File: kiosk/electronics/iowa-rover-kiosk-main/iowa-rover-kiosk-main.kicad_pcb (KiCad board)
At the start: 2 copper layers, 76.8 x 79.9 mm, 17 parts, among them J2 Barrel_Jack, J3 Conn_02x06_Odd_Even, J4 Conn_01x04, J5 Conn_02x08_Top_Bottom, J6 Conn_01x08, J7 Conn_01x03, U1 Adafruit_RFM69HCW_Breakout, U2 I50115, U3 ATtiny84-20P

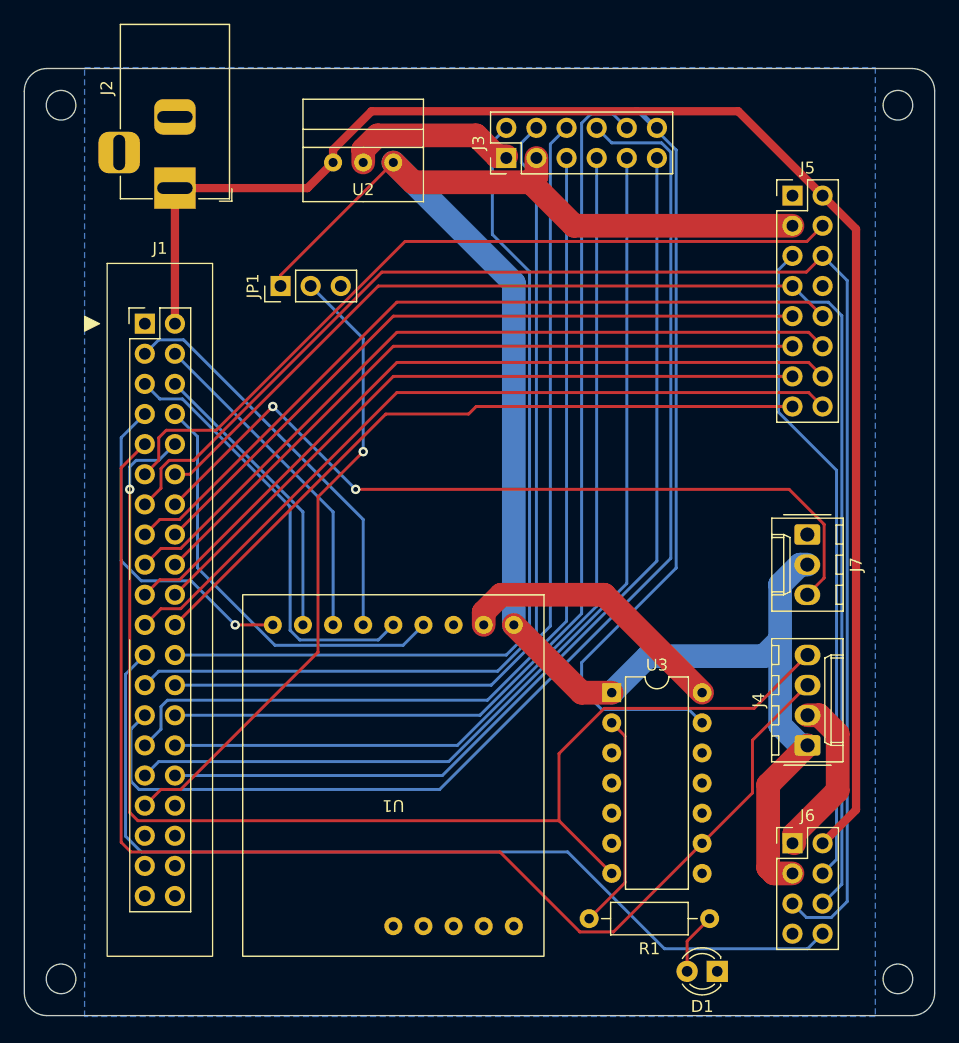
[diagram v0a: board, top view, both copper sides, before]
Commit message: initial pass at board drawings
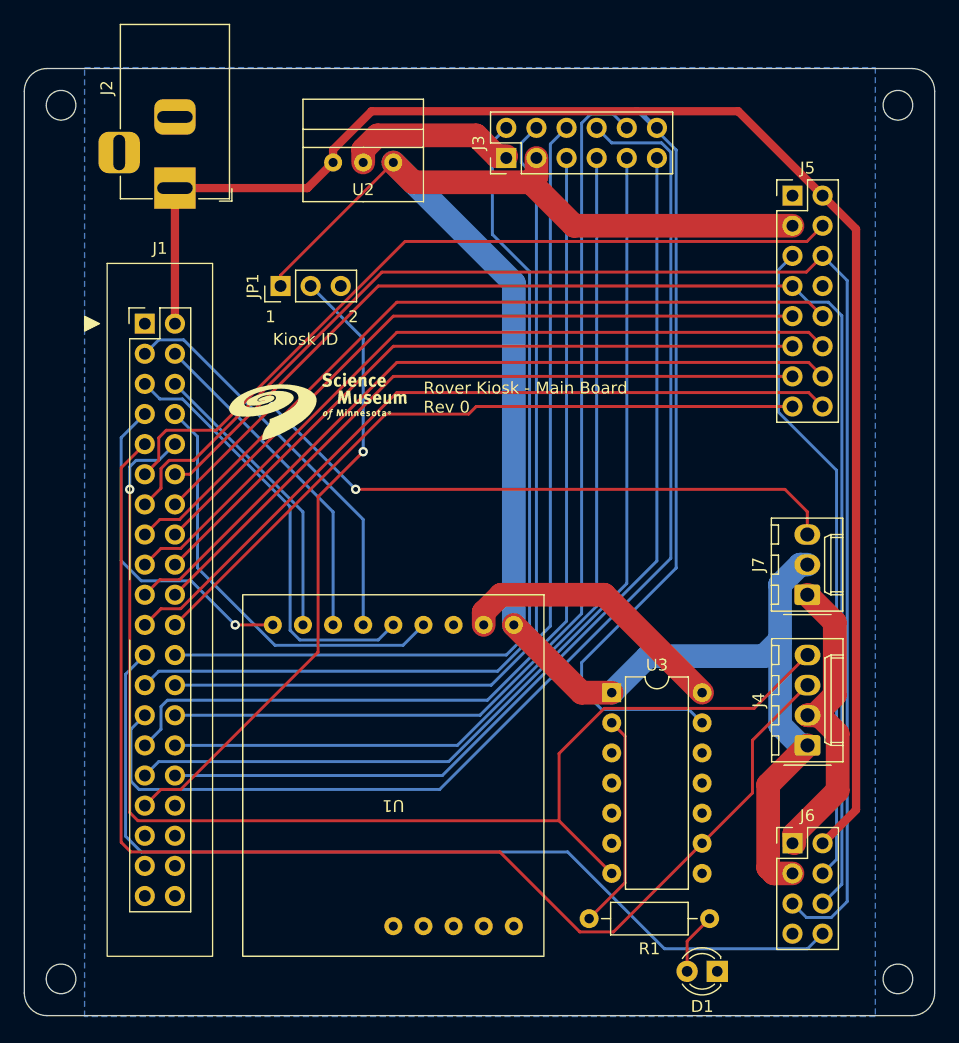
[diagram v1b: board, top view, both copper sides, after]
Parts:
- added G***: LOGO, SMM:smm-logo-15mm, F.Cu at (62.2, 75.6)
- moved J7 5.08 mm to (103.5, 91.4), turned to 90 degrees
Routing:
- net GND: track 51.8 -> 64.3 mm
- net Net-(J1-D6_NEO): track 68.8 -> 62.3 mm
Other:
- board text added: "1"
- board text added: "2"
- board text added: "Kiosk ID"
- board text added: "Rover Kiosk - Main Board Rev 0"

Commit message: update
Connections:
- U3 pad 7: /SCL -> /SDA
- U3 pad 9: /SDA -> /SCL
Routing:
- net /SDA: track 106.6 -> 74.2 mm
- net /SCL: track 106.6 -> 91.0 mm
- net +5V: track 154.1 -> 154.8 mm
- net Net-(J1-D45_RST): track 28.1 -> 28.7 mm
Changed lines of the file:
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@@
       (net 57 "unconnected-(U3-PA7-Pad6)") (pinfunction "PA7") (pintype "bidirectional+no_connect"))
     (pad "7" thru_hole oval (at 0 15.24) (size 1.6 1.6) (drill 0.8) (layers "*.Cu" "*.Mask")
-      (net 11 "/SCL") (pinfunction "PA6") (pintype "bidirectional"))
+      (net 10 "/SDA") (pinfunction "PA6") (pintype "bidirectional"))
     (pad "8" thru_hole oval (at 7.62 15.24) (size 1.6 1.6) (drill 0.8) (layers "*.Cu" "*.Mask")
       (net 58 "unconnected-(U3-PA5-Pad8)") (pinfunction "PA5") (pintype "bidirectional+no_connect"))
     (pad "9" thru_hole oval (at 7.62 12.7) (size 1.6 1.6) (drill 0.8) (layers "*.Cu" "*.Mask")
-      (net 10 "/SDA") (pinfunction "PA4") (pintype "bidirectional"))
+      (net 11 "/SCL") (pinfunction "PA4") (pintype "bidirectional"))
     (pad "10" thru_hole oval (at 7.62 10.16) (size 1.6 1.6) (drill 0.8) (layers "*.Cu" "*.Mask")
       (net 59 "unconnected-(U3-PA3-Pad10)") (pinfunction "PA3") (pintype "bidirectional+no_connect"))
@@
   (segment (start 58.42 93.98) (end 55.335 93.98) (width 0.25) (layer "F.Cu") (net 8))
   (via (at 55.245 93.98) (size 0.8) (drill 0.4) (layers "F.Cu" "B.Cu") (net 8))
-  (segment (start 55.245 93.98) (end 51.53 90.265) (width 0.25) (layer "B.Cu") (net 8))
-  (segment (start 47.328299 90.265) (end 45.63 88.566701) (width 0.25) (layer "B.Cu") (net 8))
-  (segment (start 45.63 78.195) (end 47.625 76.2) (width 0.25) (layer "B.Cu") (net 8))
-  (segment (start 45.63 88.566701) (end 45.63 78.195) (width 0.25) (layer "B.Cu") (net 8))
-  (segment (start 51.53 90.265) (end 47.328299 90.265) (width 0.25) (layer "B.Cu") (net 8))
+  (segment (start 47.233299 90.17) (end 51.435 90.17) (width 0.25) (layer "B.Cu") (net 8))
+  (segment (start 51.435 90.17) (end 55.245 93.98) (width 0.25) (layer "B.Cu") (net 8))
+  (segment (start 47.625 76.2) (end 44.995 78.83) (width 0.25) (layer "B.Cu") (net 8))
+  (segment (start 44.995 78.83) (end 44.995 87.931701) (width 0.25) (layer "B.Cu") (net 8))
+  (segment (start 44.995 87.931701) (end 47.233299 90.17) (width 0.25) (layer "B.Cu") (net 8))
   (segment (start 69.4 95.7) (end 58.602749 95.7) (width 0.25) (layer "B.Cu") (net 9))
   (segment (start 71.12 93.98) (end 69.4 95.7) (width 0.25) (layer "B.Cu") (net 9))
@@
   (segment (start 58.602749 95.7) (end 52.069302 89.166553) (width 0.25) (layer "B.Cu") (net 9))
   (segment (start 52.069302 89.166553) (end 52.069302 78.104302) (width 0.25) (layer "B.Cu") (net 9))
-  (segment (start 45.63 112.305) (end 46.45 113.125) (width 0.25) (layer "F.Cu") (net 10))
-  (segment (start 98.86 108.15) (end 98.86 103.705) (width 0.25) (layer "F.Cu") (net 10))
-  (segment (start 84.31 119.87) (end 87.14 119.87) (width 0.25) (layer "F.Cu") (net 10))
-  (segment (start 47.625 78.74) (end 45.63 80.735) (width 0.25) (layer "F.Cu") (net 10))
-  (segment (start 98.86 103.705) (end 103.505 99.06) (width 0.25) (layer "F.Cu") (net 10))
-  (segment (start 45.63 80.735) (end 45.63 112.305) (width 0.25) (layer "F.Cu") (net 10))
-  (segment (start 46.45 113.125) (end 77.565 113.125) (width 0.25) (layer "F.Cu") (net 10))
-  (segment (start 94.615 112.395) (end 98.86 108.15) (width 0.25) (layer "F.Cu") (net 10))
-  (segment (start 77.565 113.125) (end 84.31 119.87) (width 0.25) (layer "F.Cu") (net 10))
-  (segment (start 87.14 119.87) (end 94.615 112.395) (width 0.25) (layer "F.Cu") (net 10))
-  (segment (start 82.55 110.49) (end 86.995 114.935) (width 0.25) (layer "F.Cu") (net 11))
-  (segment (start 86.36 101.02) (end 99.005 101.02) (width 0.25) (layer "F.Cu") (net 11))
-  (segment (start 82.55 110.49) (end 82.55 104.83) (width 0.25) (layer "F.Cu") (net 11))
-  (segment (start 46.355 82.55) (end 46.355 109.801701) (width 0.25) (layer "F.Cu") (net 11))
-  (segment (start 99.005 101.02) (end 103.505 96.52) (width 0.25) (layer "F.Cu") (net 11))
-  (segment (start 46.355 109.801701) (end 47.043299 110.49) (width 0.25) (layer "F.Cu") (net 11))
-  (segment (start 82.55 104.83) (end 86.36 101.02) (width 0.25) (layer "F.Cu") (net 11))
-  (segment (start 47.043299 110.49) (end 82.55 110.49) (width 0.25) (layer "F.Cu") (net 11))
-  (via (at 46.355 82.55) (size 0.8) (drill 0.4) (layers "F.Cu" "B.Cu") (net 11))
-  (segment (start 48.8 80.105) (end 50.165 78.74) (width 0.25) (layer "B.Cu") (net 11))
-  (segment (start 46.355 80.645) (end 46.895 80.105) (width 0.25) (layer "B.Cu") (net 11))
-  (segment (start 46.355 82.55) (end 46.355 80.645) (width 0.25) (layer "B.Cu") (net 11))
-  (segment (start 46.895 80.105) (end 48.8 80.105) (width 0.25) (layer "B.Cu") (net 11))
+  (segment (start 82.645 110.585) (end 86.995 114.935) (width 0.25) (layer "F.Cu") (net 10))
+  (segment (start 47.625 78.74) (end 46.45 79.915) (width 0.25) (layer "F.Cu") (net 10))
+  (segment (start 46.45 109.706701) (end 47.328299 110.585) (width 0.25) (layer "F.Cu") (net 10))
+  (segment (start 46.45 79.915) (end 46.45 109.706701) (width 0.25) (layer "F.Cu") (net 10))
+  (segment (start 47.328299 110.585) (end 82.645 110.585) (width 0.25) (layer "F.Cu") (net 10))
+  (segment (start 73.832251 112.935) (end 47.138299 112.935) (width 0.25) (layer "F.Cu") (net 11))
+  (segment (start 87.14 119.87) (end 80.767251 119.87) (width 0.25) (layer "F.Cu") (net 11))
+  (segment (start 94.615 112.395) (end 87.14 119.87) (width 0.25) (layer "F.Cu") (net 11))
+  (segment (start 80.767251 119.87) (end 73.832251 112.935) (width 0.25) (layer "F.Cu") (net 11))
+  (segment (start 45.72 111.516701) (end 45.72 82.55) (width 0.25) (layer "F.Cu") (net 11))
+  (segment (start 47.138299 112.935) (end 45.72 111.516701) (width 0.25) (layer "F.Cu") (net 11))
+  (via (at 45.72 82.55) (size 0.8) (drill 0.4) (layers "F.Cu" "B.Cu") (net 11))
+  (segment (start 47.233299 80.01) (end 48.895 80.01) (width 0.25) (layer "B.Cu") (net 11))
+  (segment (start 45.72 81.523299) (end 47.233299 80.01) (width 0.25) (layer "B.Cu") (net 11))
+  (segment (start 45.72 82.55) (end 45.72 81.523299) (width 0.25) (layer "B.Cu") (net 11))
+  (segment (start 48.895 80.01) (end 50.165 78.74) (width 0.25) (layer "B.Cu") (net 11))
   (segment (start 49.435 77.565) (end 48.8 78.2) (width 0.25) (layer "F.Cu") (net 12))
   (segment (start 48.8 78.2) (end 48.8 80.105) (width 0.25) (layer "F.Cu") (net 12))
@@
   (segment (start 84.455 99.695) (end 78.74 93.98) (width 2) (layer "F.Cu") (net 42))
   (segment (start 100.185 114.445) (end 100.675 114.935) (width 2) (layer "F.Cu") (net 42))
-  (segment (start 101.19 102.437422) (end 102.892578 104.14) (width 2) (layer "B.Cu") (net 42))
-  (segment (start 102.872578 88.9) (end 101.19 90.582578) (width 2) (layer "B.Cu") (net 42))
+  (segment (start 102.892578 104.14) (end 99.825 101.072422) (width 2) (layer "B.Cu") (net 42))
   (segment (start 86.995 99.695) (end 90.075 96.615) (width 2) (layer "B.Cu") (net 42))
-  (segment (start 99.825 96.615) (end 101.19 95.25) (width 2) (layer "B.Cu") (net 42))
+  (segment (start 99.825 101.072422) (end 99.825 96.615) (width 2) (layer "B.Cu") (net 42))
+  (segment (start 99.825 89.465) (end 100.39 88.9) (width 2) (layer "B.Cu") (net 42))
   (segment (start 68.58 54.991) (end 78.74 65.151) (width 2) (layer "B.Cu") (net 42))
   (segment (start 90.075 96.615) (end 99.825 96.615) (width 2) (layer "B.Cu") (net 42))
-  (segment (start 102.892578 104.14) (end 103.505 104.14) (width 2) (layer "B.Cu") (net 42))
-  (segment (start 101.19 95.25) (end 101.19 102.437422) (width 2) (layer "B.Cu") (net 42))
+  (segment (start 99.825 96.615) (end 99.825 89.465) (width 2) (layer "B.Cu") (net 42))
+  (segment (start 100.39 88.9) (end 103.485 88.9) (width 2) (layer "B.Cu") (net 42))
   (segment (start 78.74 65.151) (end 78.74 93.98) (width 2) (layer "B.Cu") (net 42))
-  (segment (start 103.485 88.9) (end 102.872578 88.9) (width 2) (layer "B.Cu") (net 42))
-  (segment (start 101.19 90.582578) (end 101.19 95.25) (width 2) (layer "B.Cu") (net 42))
+  (segment (start 103.505 104.14) (end 102.892578 104.14) (width 2) (layer "B.Cu") (net 42))
   (segment (start 92.43 89.18) (end 84.455 97.155) (width 0.25) (layer "B.Cu") (net 43))
   (segment (start 84.455 99.405) (end 86.16 101.11) (width 0.25) (layer "B.Cu") (net 43))

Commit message: add gerbers and initial radio code
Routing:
- net /SDA: track 74.2 -> 114.0 mm
- net /SCL: track 91.0 -> 110.6 mm
- net Net-(J3-Pin_12): track 67.6 -> 62.6 mm
- net GND: track 64.3 -> 65.0 mm
- net +12V: track 129.2 -> 129.8 mm
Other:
- board text added: "Lamps"
- board text added: "Level Buttons"
- board text added: "Neo"
- board text added: "Programmer"
- board text added: "RFID"
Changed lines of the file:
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@@
       (plot_on_all_layers_selection 0x0000000_00000000)
       (disableapertmacros false)
-      (usegerberextensions false)
+      (usegerberextensions true)
       (usegerberattributes true)
       (usegerberadvancedattributes true)
@@
       (plotinvisibletext false)
       (sketchpadsonfab false)
-      (subtractmaskfromsilk false)
+      (subtractmaskfromsilk true)
       (outputformat 1)
       (mirror false)
-      (drillshape 1)
+      (drillshape 0)
       (scaleselection 1)
-      (outputdirectory "")
+      (outputdirectory "gerber/")
     )
   )
@@
     (fp_line (start 6.35 2.88) (end 6.35 -2.92)
       (stroke (width 0.1) (type solid)) (layer "F.Fab"))
-    (pad "1" thru_hole roundrect (at 0 0 90) (size 1.74 2.19) (drill 1.19) (layers "*.Cu" "*.Mask") (roundrect_rratio 0.143678)
+    (pad "1" thru_hole roundrect (at 0 0 90) (size 1.74 2.19) (drill 1.19) (layers "*.Cu" "*.Mask") (roundrect_rratio 0.1436781609)
       (net 1 "GND") (pinfunction "Pin_1") (pintype "passive"))
     (pad "2" thru_hole oval (at 2.54 0 90) (size 1.74 2.19) (drill 1.19) (layers "*.Cu" "*.Mask")
@@
     (fp_line (start 8.89 2.88) (end 8.89 -2.92)
       (stroke (width 0.1) (type solid)) (layer "F.Fab"))
-    (pad "1" thru_hole roundrect (at 0 0 90) (size 1.74 2.19) (drill 1.19) (layers "*.Cu" "*.Mask") (roundrect_rratio 0.143678)
+    (pad "1" thru_hole roundrect (at 0 0 90) (size 1.74 2.19) (drill 1.19) (layers "*.Cu" "*.Mask") (roundrect_rratio 0.1436781609)
       (net 42 "+5V") (pinfunction "Pin_1") (pintype "passive"))
     (pad "2" thru_hole oval (at 2.54 0 90) (size 1.74 2.19) (drill 1.19) (layers "*.Cu" "*.Mask")
@@
   (gr_arc (start 112.317962 47.067038) (mid 113.665 47.625) (end 114.222962 48.972038)
     (stroke (width 0.1) (type default)) (layer "Edge.Cuts"))
+  (gr_text "Neo" (at 100.33 83.82) (layer "F.SilkS")
+    (effects (font (size 1 1) (thickness 0.1)) (justify left bottom))
+  )
+  (gr_text "Lamps\n" (at 101.6 125.73) (layer "F.SilkS")
+    (effects (font (size 1 1) (thickness 0.1)) (justify left bottom))
+  )
+  (gr_text "Level Buttons" (at 97.79 73.66 90) (layer "F.SilkS")
+    (effects (font (size 1 1) (thickness 0.1)) (justify left bottom))
+  )
   (gr_text "1" (at 57.785 68.58) (layer "F.SilkS")
     (effects (font (size 1 1) (thickness 0.15)) (justify left bottom))
@@
     (effects (font (size 1 1) (thickness 0.15)) (justify left bottom))
   )
+  (gr_text "Programmer" (at 80.01 58.42) (layer "F.SilkS")
+    (effects (font (size 1 1) (thickness 0.1)) (justify left bottom))
+  )
   (gr_text "2\n" (at 64.77 68.58) (layer "F.SilkS")
     (effects (font (size 1 1) (thickness 0.15)) (justify left bottom))
@@
     (effects (font (size 1 1) (thickness 0.15)) (justify left bottom))
   )
+  (gr_text "RFID\n" (at 100.33 106.68 90) (layer "F.SilkS")
+    (effects (font (size 1 1) (thickness 0.1)) (justify left bottom))
+  )
   (segment (start 86.36 91.44) (end 94.615 99.695) (width 2) (layer "F.Cu") (net 1))
-  (segment (start 104.117422 101.6) (end 105.8 99.917422) (width 2) (layer "F.Cu") (net 1))
   (segment (start 76.2 92.90237) (end 77.66237 91.44) (width 2) (layer "F.Cu") (net 1))
   (segment (start 103.505 101.6) (end 104.48061 101.6) (width 2) (layer "F.Cu") (net 1))
-  (segment (start 105.8 93.755) (end 103.485 91.44) (width 2) (layer "F.Cu") (net 1))
   (segment (start 66.04 53.91337) (end 67.24837 52.705) (width 2) (layer "F.Cu") (net 1))
   (segment (start 76.2 93.98) (end 76.2 92.90237) (width 2) (layer "F.Cu") (net 1))
@@
   (segment (start 77.66237 91.44) (end 86.36 91.44) (width 2) (layer "F.Cu") (net 1))
   (segment (start 66.04 54.991) (end 66.04 53.91337) (width 2) (layer "F.Cu") (net 1))
+  (segment (start 106.735 94.69) (end 103.485 91.44) (width 2) (layer "F.Cu") (net 1))
   (segment (start 106.045 103.16439) (end 106.045 107.95) (width 2) (layer "F.Cu") (net 1))
-  (segment (start 105.8 99.917422) (end 105.8 93.755) (width 2) (layer "F.Cu") (net 1))
+  (segment (start 104.117422 101.6) (end 106.735 98.982422) (width 2) (layer "F.Cu") (net 1))
   (segment (start 103.505 101.6) (end 104.117422 101.6) (width 2) (layer "F.Cu") (net 1))
   (segment (start 75.565 52.705) (end 77.32 54.46) (width 2) (layer "F.Cu") (net 1))
+  (segment (start 106.735 98.982422) (end 106.735 94.69) (width 2) (layer "F.Cu") (net 1))
   (segment (start 77.32 54.46) (end 78.105 54.46) (width 2) (layer "F.Cu") (net 1))
   (segment (start 106.045 107.95) (end 102.385 111.61) (width 2) (layer "F.Cu") (net 1))
@@
   (segment (start 93.35 120.645) (end 95.25 118.745) (width 0.25) (layer "F.Cu") (net 2))
   (segment (start 97.66 50.67) (end 104.775 57.785) (width 0.7) (layer "F.Cu") (net 3))
-  (segment (start 107.595 109.575) (end 104.775 112.395) (width 0.7) (layer "F.Cu") (net 3))
-  (segment (start 104.775 57.785) (end 107.595 60.605) (width 0.7) (layer "F.Cu") (net 3))
+  (segment (start 108.285 61.295) (end 108.285 108.885) (width 0.7) (layer "F.Cu") (net 3))
+  (segment (start 104.775 57.785) (end 108.285 61.295) (width 0.7) (layer "F.Cu") (net 3))
   (segment (start 50.165 57.15) (end 50.165 68.58) (width 0.7) (layer "F.Cu") (net 3))
+  (segment (start 108.285 108.885) (end 104.775 112.395) (width 0.7) (layer "F.Cu") (net 3))
   (segment (start 61.341 57.15) (end 63.5 54.991) (width 0.7) (layer "F.Cu") (net 3))
-  (segment (start 107.595 60.605) (end 107.595 109.575) (width 0.7) (layer "F.Cu") (net 3))
   (segment (start 50.165 57.15) (end 61.341 57.15) (width 0.7) (layer "F.Cu") (net 3))
   (segment (start 63.5 53.91337) (end 66.74337 50.67) (width 0.7) (layer "F.Cu") (net 3))
@@
   (segment (start 58.602749 95.7) (end 52.069302 89.166553) (width 0.25) (layer "B.Cu") (net 9))
   (segment (start 52.069302 89.166553) (end 52.069302 78.104302) (width 0.25) (layer "B.Cu") (net 9))
+  (segment (start 85.87 113.81) (end 85.87 101.51) (width 0.25) (layer "F.Cu") (net 10))
+  (segment (start 85.87 101.51) (end 86.36 101.02) (width 0.25) (layer "F.Cu") (net 10))
+  (segment (start 105.41 97.155) (end 103.505 99.06) (width 0.25) (layer "F.Cu") (net 10))
   (segment (start 82.645 110.585) (end 86.995 114.935) (width 0.25) (layer "F.Cu") (net 10))
+  (segment (start 105.41 96.510015) (end 105.41 97.155) (width 0.25) (layer "F.Cu") (net 10))
   (segment (start 47.625 78.74) (end 46.45 79.915) (width 0.25) (layer "F.Cu") (net 10))
   (segment (start 46.45 109.706701) (end 47.328299 110.585) (width 0.25) (layer "F.Cu") (net 10))
+  (segment (start 86.995 114.935) (end 85.87 113.81) (width 0.25) (layer "F.Cu") (net 10))
+  (segment (start 95.83 101.02) (end 101.525 95.325) (width 0.25) (layer "F.Cu") (net 10))
   (segment (start 46.45 79.915) (end 46.45 109.706701) (width 0.25) (layer "F.Cu") (net 10))
+  (segment (start 101.525 95.325) (end 104.224985 95.325) (width 0.25) (layer "F.Cu") (net 10))
   (segment (start 47.328299 110.585) (end 82.645 110.585) (width 0.25) (layer "F.Cu") (net 10))
+  (segment (start 86.36 101.02) (end 95.83 101.02) (width 0.25) (layer "F.Cu") (net 10))
+  (segment (start 104.224985 95.325) (end 105.41 96.510015) (width 0.25) (layer "F.Cu") (net 10))
   (segment (start 73.832251 112.935) (end 47.138299 112.935) (width 0.25) (layer "F.Cu") (net 11))
+  (segment (start 98.86 108.15) (end 94.615 112.395) (width 0.25) (layer "F.Cu") (net 11))
+  (segment (start 98.86 101.165) (end 98.86 108.15) (width 0.25) (layer "F.Cu") (net 11))
   (segment (start 87.14 119.87) (end 80.767251 119.87) (width 0.25) (layer "F.Cu") (net 11))
   (segment (start 94.615 112.395) (end 87.14 119.87) (width 0.25) (layer "F.Cu") (net 11))
+  (segment (start 103.505 96.52) (end 98.86 101.165) (width 0.25) (layer "F.Cu") (net 11))
   (segment (start 80.767251 119.87) (end 73.832251 112.935) (width 0.25) (layer "F.Cu") (net 11))
   (segment (start 45.72 111.516701) (end 45.72 82.55) (width 0.25) (layer "F.Cu") (net 11))
@@
   (segment (start 78.74 65.151) (end 78.74 93.98) (width 2) (layer "B.Cu") (net 42))
   (segment (start 103.505 104.14) (end 102.892578 104.14) (width 2) (layer "B.Cu") (net 42))
+  (segment (start 84.455 97.155) (end 84.455 99.405) (width 0.25) (layer "B.Cu") (net 43))
   (segment (start 92.43 89.18) (end 84.455 97.155) (width 0.25) (layer "B.Cu") (net 43))
   (segment (start 84.455 99.405) (end 86.16 101.11) (width 0.25) (layer "B.Cu") (net 43))
-  (segment (start 89.18 50.445) (end 88.938097 50.445) (width 0.25) (layer "B.Cu") (net 43))
-  (segment (start 92.43 53.936903) (end 92.43 89.18) (width 0.25) (layer "B.Cu") (net 43))
   (segment (start 93.49 101.11) (end 94.615 102.235) (width 0.25) (layer "B.Cu") (net 43))
   (segment (start 86.16 101.11) (end 93.49 101.11) (width 0.25) (layer "B.Cu") (net 43))
-  (segment (start 90.805 52.07) (end 89.18 50.445) (width 0.25) (layer "B.Cu") (net 43))
-  (segment (start 84.455 97.155) (end 84.455 99.405) (width 0.25) (layer "B.Cu") (net 43))
-  (segment (start 88.938097 50.445) (end 92.43 53.936903) (width 0.25) (layer "B.Cu") (net 43))
+  (segment (start 92.43 53.695) (end 92.43 89.18) (width 0.25) (layer "B.Cu") (net 43))
+  (segment (start 90.805 52.07) (end 92.43 53.695) (width 0.25) (layer "B.Cu") (net 43))
   (segment (start 105.95 80.941701) (end 101.06 76.051701) (width 0.25) (layer "B.Cu") (net 44))
   (segment (start 105.95 113.76) (end 105.95 80.941701) (width 0.25) (layer "B.Cu") (net 44))
